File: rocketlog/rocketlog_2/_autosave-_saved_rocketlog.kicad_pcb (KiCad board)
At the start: 2 copper layers, 26 parts, among them J1 Conn_01x05_Female, J2 Micro_SD_Card, J3 BUS CONN, U1 DSPIC33EP512GP502, U2 MCP2562, U3 INA180, U4 AP2114H-3.3, Y1 Crystal

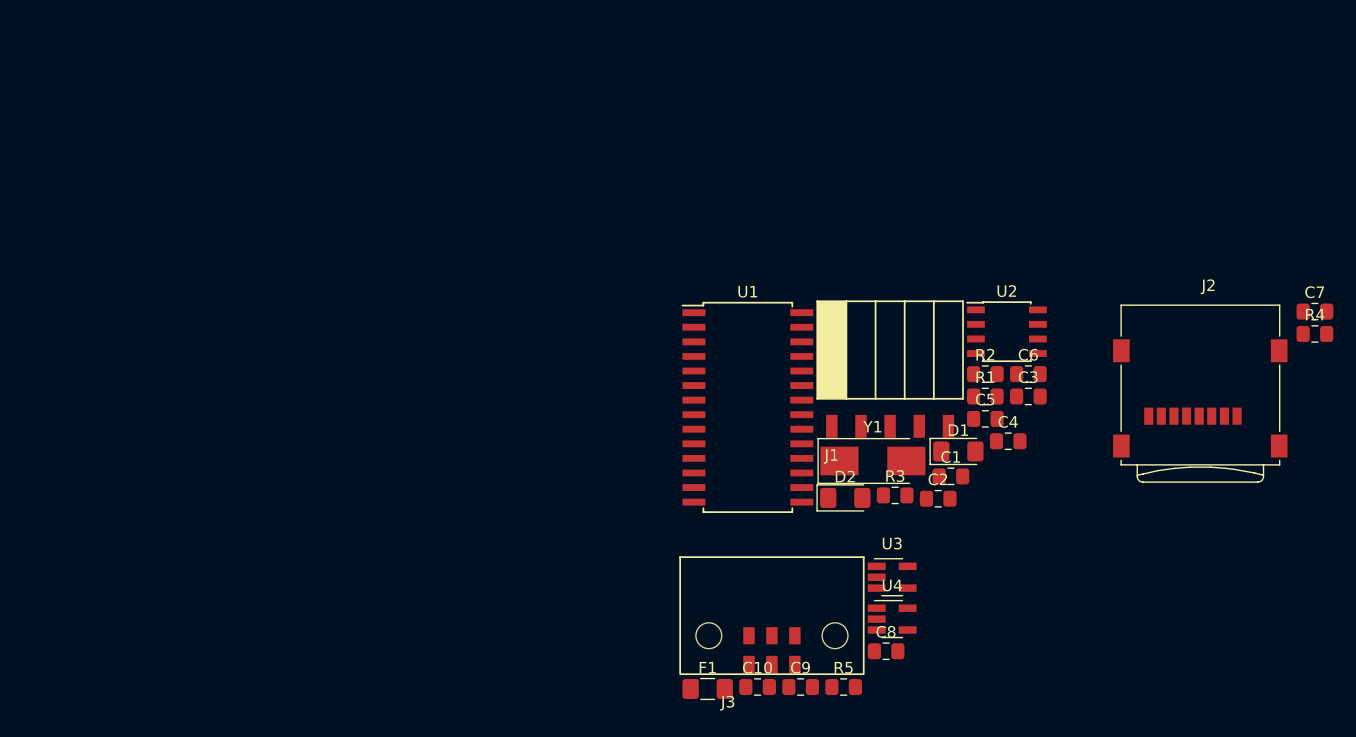
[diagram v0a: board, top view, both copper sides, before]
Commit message: logger 2 component layout for review
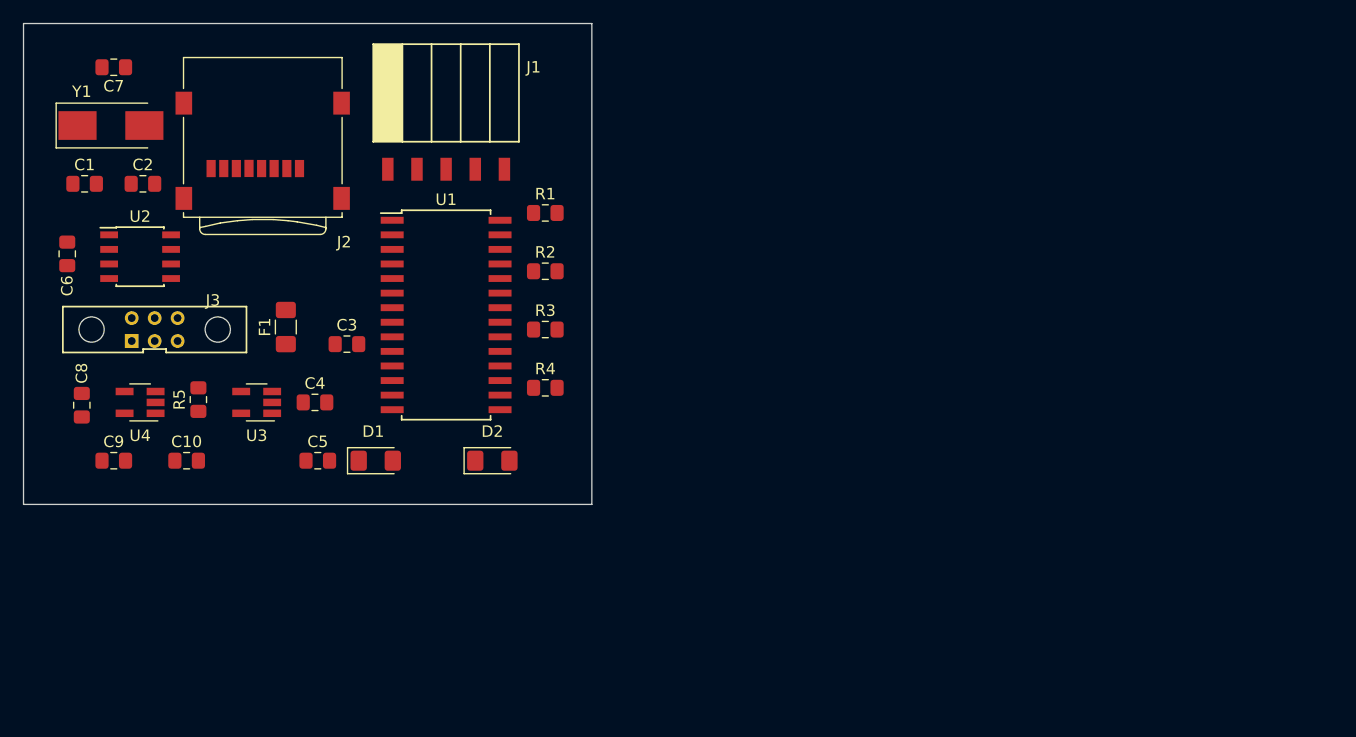
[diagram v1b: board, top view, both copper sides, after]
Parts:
- J3: footprint canhw_footprints:connector_Harwin_M80-5420642 -> canhw_footprints:connector_Harwin_M80-5000642
- moved C7 106.8 mm to (72.6, 58.4), turned to 180 degrees
- moved J2 84.5 mm to (78.7, 69.8)
- moved C6 84.4 mm to (68.6, 74.7), turned to 90 degrees
- moved C1 79.7 mm to (70.1, 68.6)
- moved U2 75.8 mm to (74.9, 74.9)
- moved C2 74.5 mm to (75.2, 68.6)
- moved C8 73.3 mm to (69.8, 87.9), turned to 90 degrees
- moved Y1 72.6 mm to (72.4, 63.5)
- moved U4 68.2 mm to (74.9, 87.6), turned to 180 degrees
- moved R4 67.2 mm to (110.2, 86.4)
- moved C9 63.0 mm to (72.6, 92.7)
- moved J3 61.6 mm to (76.2, 81.3)
- moved R5 61.6 mm to (80.0, 87.4), turned to 90 degrees
- moved C4 60.5 mm to (90.2, 87.6)
- moved C3 59.6 mm to (93.0, 82.5)
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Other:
- board outline added: 49.5 x 41.9 mm
- net class Default: clearance 0.2 -> 0.254; trace_width 0.25 -> 0.440004; via_dia 0.8 -> 0.762; via_drill 0.4 -> 0.381
- rule pad_to_mask_clearance: 0 -> 0.0508
- rule trace_clearance: 0.2 -> 0.254
- rule trace_min: 0.2 -> 0.44
- rule via_min_drill: 0.3 -> 0.381
- rule via_min_size: 0.4 -> 0.381
